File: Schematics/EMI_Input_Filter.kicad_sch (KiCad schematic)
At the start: 3 parts

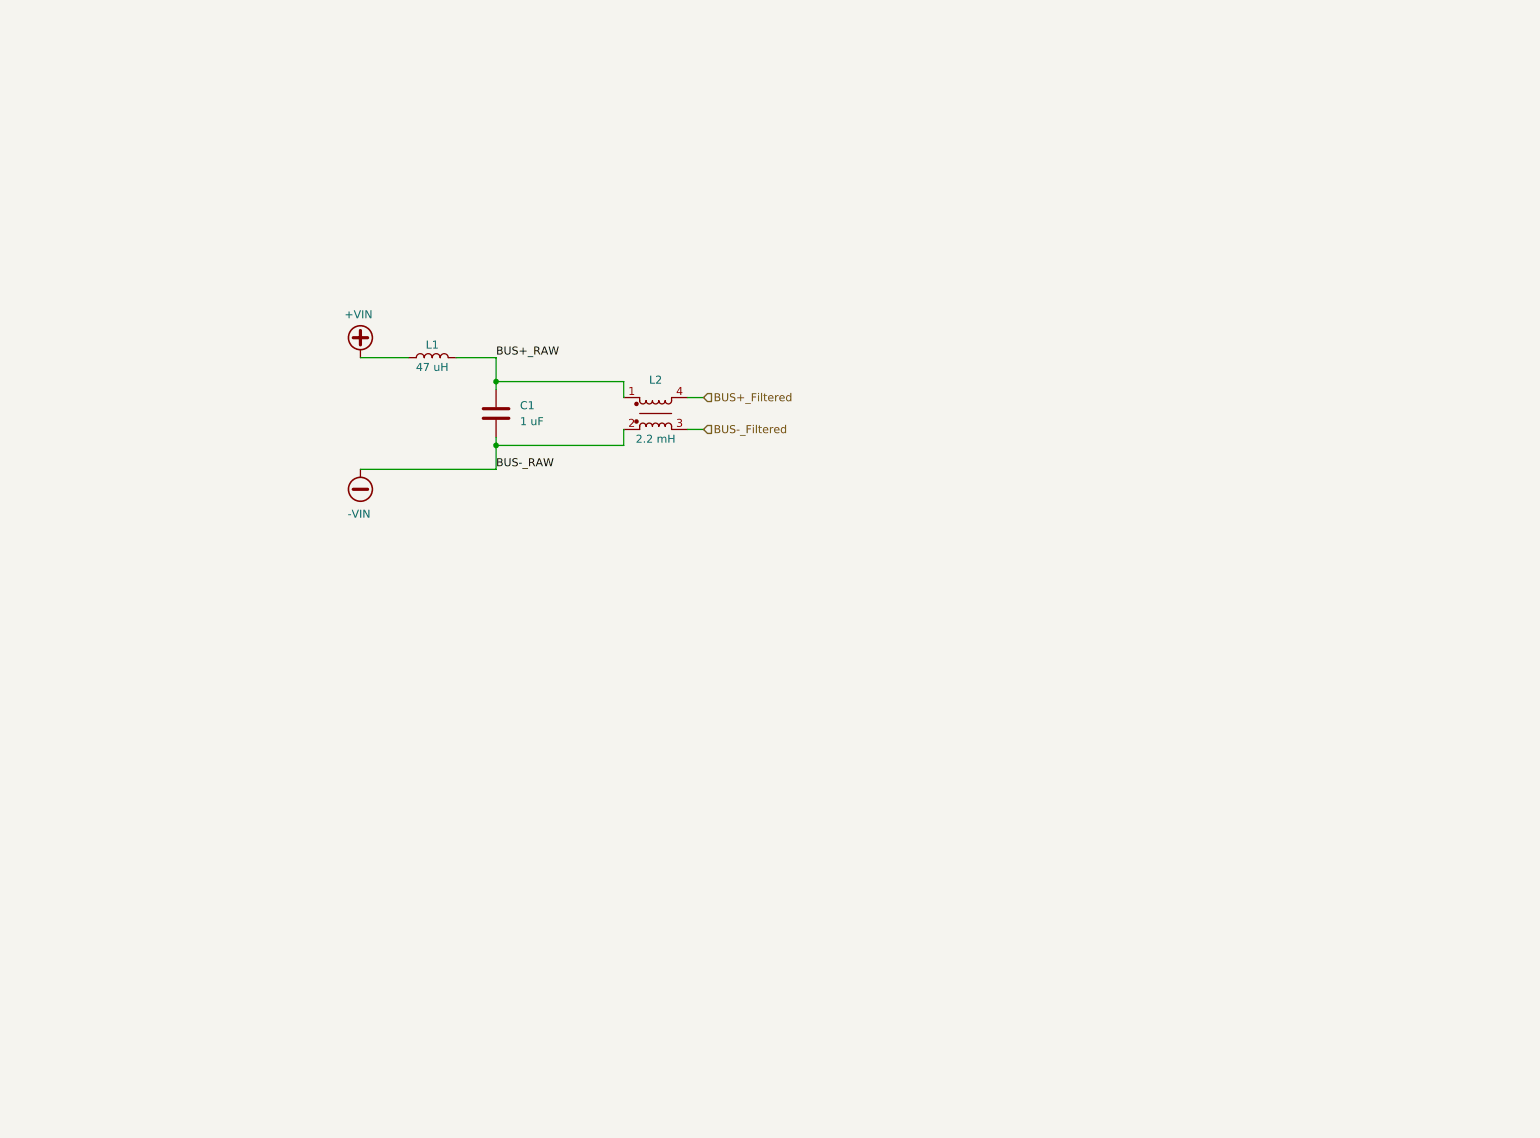
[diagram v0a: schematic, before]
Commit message: [SiC Inverter WIP]
- Deleted backup files
- changed symbol and footprint lib locations
- added text discription explaining the DC link sub sheet and emi  input
  filter subsheet
- Added Vin+,- Black and Red connector
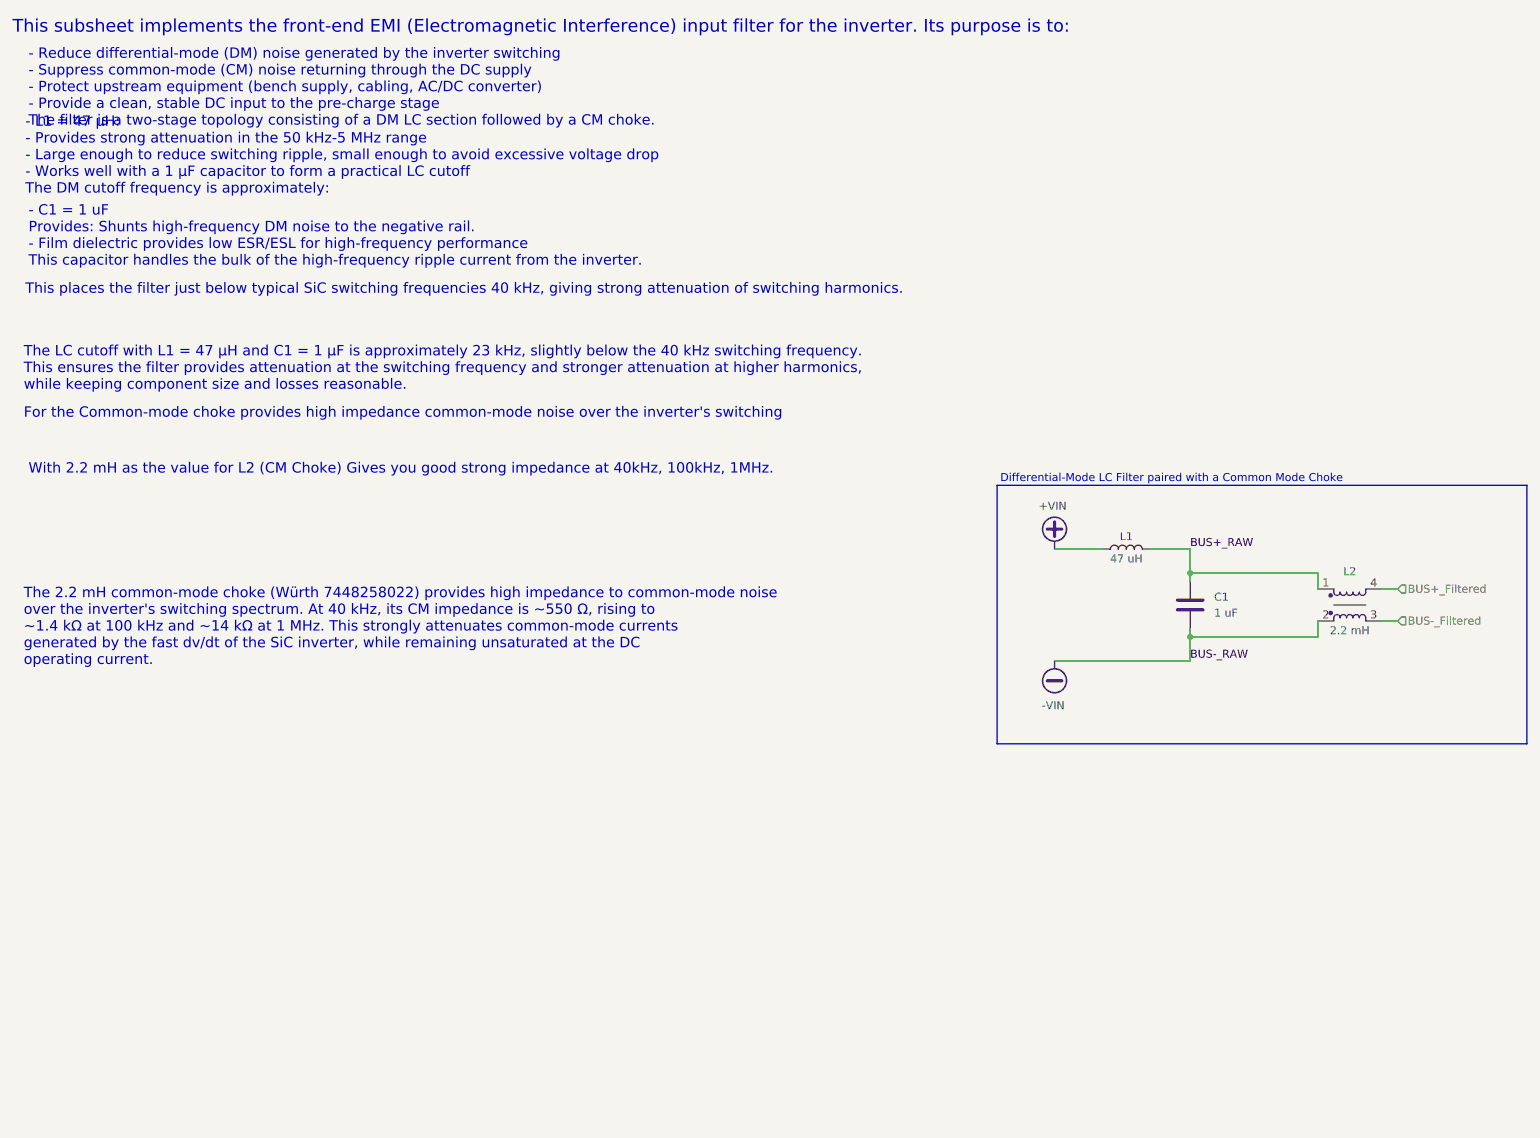
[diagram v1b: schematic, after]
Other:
- note added: "- C1 = 1 uF Provides: Shunts high‑frequency DM noise to the negative rail. - Film dielectric provides low ESR/ESL for high‑frequency performance This capacitor handles the bulk of the high‑frequency ripple current from the inverter."
- note added: "- L1 = 47 µH: - Provides strong attenuation in the 50 kHz-5 MHz range - Large enough to reduce switching ripple, small enough to avoid excessive voltage drop - Works well with a 1 µF capacitor to form a practical LC cutoff The DM cutoff frequency is approximately: This places the filter just below typical SiC switching frequencies 40 kHz, giving strong attenuation of switching harmonics."
- note added: "- Reduce differential‑mode (DM) noise generated by the inverter switching - Suppress common‑mode (CM) noise returning through the DC supply - Protect upstream equipment (bench supply, cabling, AC/DC converter) - Provide a clean, stable DC input to the pre‑charge stage The filter is a two‑stage topology consisting of a DM LC section followed by a CM choke."
- note added: "Differential-Mode LC Filter paired with a Common Mode Choke"
- note added: "For the Common-mode choke provides high impedance common-mode noise over the inverter's switching"
- note added: "The 2.2 mH common‑mode choke (Würth 7448258022) provides high impedance to common‑mode noise over the inverter's switching spectrum. At 40 kHz, its CM impedance is ~550 Ω, rising to ~1.4 kΩ at 100 kHz and ~14 kΩ at 1 MHz. This strongly attenuates common‑mode currents generated by the fast dv/dt of the SiC inverter, while remaining unsaturated at the DC operating current."
- note added: "The LC cutoff with L1 = 47 µH and C1 = 1 µF is approximately 23 kHz, slightly below the 40 kHz switching frequency. This ensures the filter provides attenuation at the switching frequency and stronger attenuation at higher harmonics, while keeping component size and losses reasonable."
- note added: "This subsheet implements the front‑end EMI (Electromagnetic Interference) input filter for the inverter. Its purpose is to:"
- note added: "With 2.2 mH as the value for L2 (CM Choke) Gives you good strong impedance at 40kHz, 100kHz, 1MHz."
- moved on the sheet: C1, L1, L2

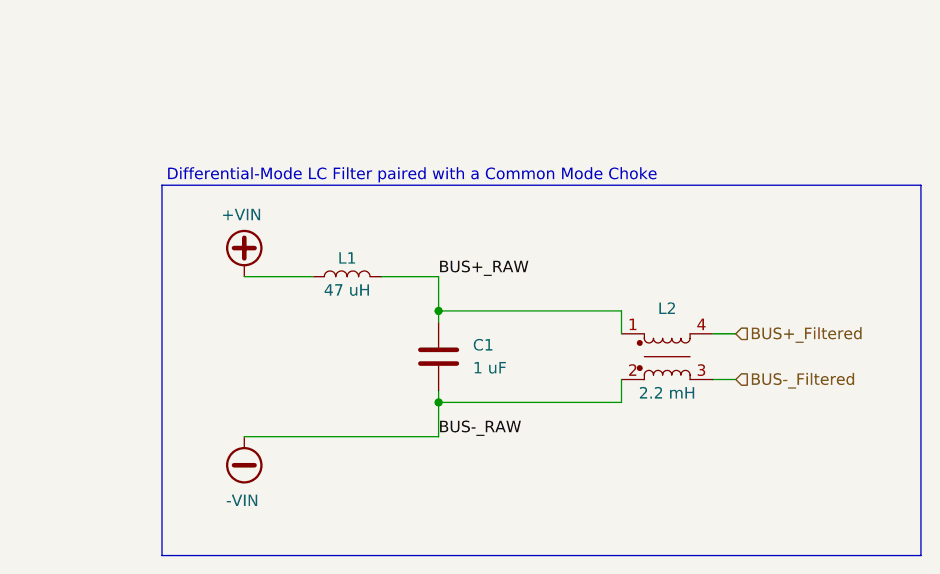
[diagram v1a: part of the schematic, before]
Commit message: Work in progress
- Added new parts to PCB to check 3d models
- Added input protection sheet
- Added TVS, N-Channel MOSFET, Zensor, and resiters to protection
  circuit
- Added datasheets for new parts
- Added circuit GND
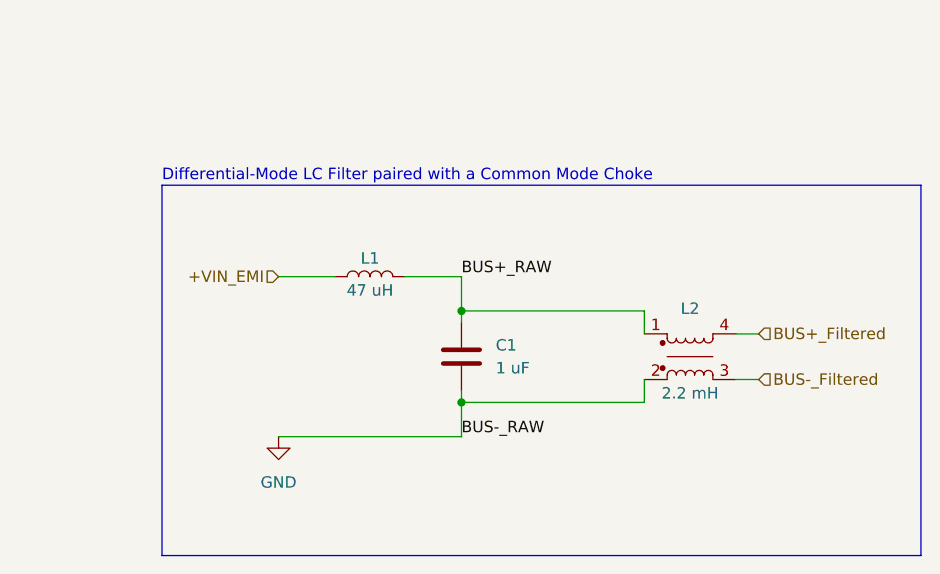
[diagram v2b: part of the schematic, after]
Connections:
- net +VIN renamed +VIN_EMI
- net -VIN renamed GND
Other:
- moved on the sheet: C1, L1, L2

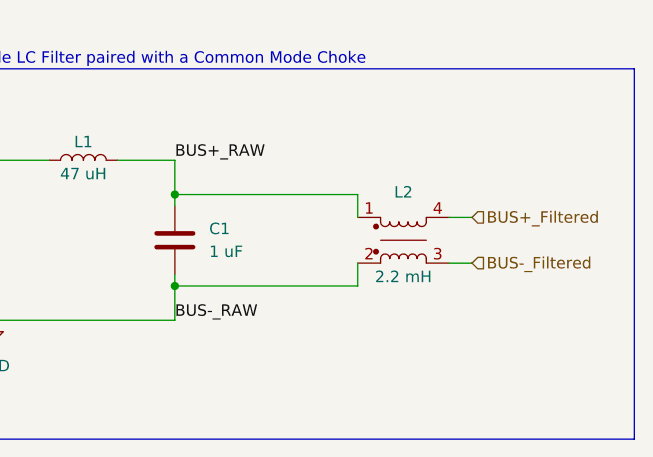
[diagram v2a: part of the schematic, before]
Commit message: [WIP - SIC Inverter]
- Added 3d models for 3 parts
- Added 3 new footprints for the 3 added parts
- Changed footprint 23AH8785 and 86 Black and Red
- Finished WIP with EMI, Input Protection, and Precharge
- Added datasheet
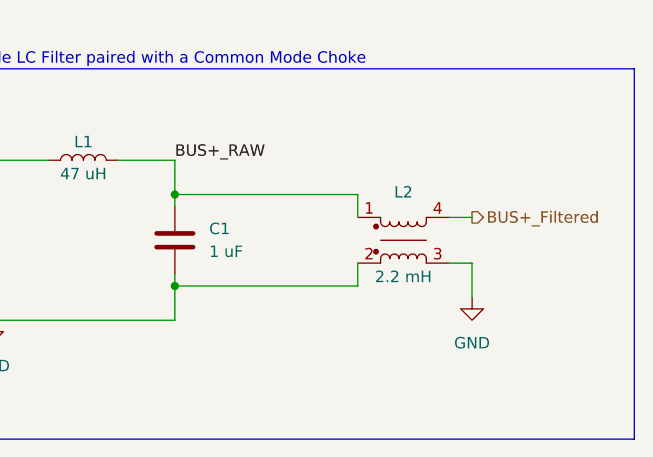
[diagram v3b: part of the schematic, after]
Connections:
- net BUS-_Filtered is gone; now on net GND: L2.3
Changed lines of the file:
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@@
+		)
+	)
+	(wire
+		(pts
+			(xy 236.22 114.3) (xy 236.22 110.49)
+		)
+		(stroke
+			(width 0)
+			(type default)
 		)
 	)
@@
 		)
 	)
-	(label "BUS-_RAW"
-		(at 203.2 116.84 0)
-		(effects
-			(font
-				(size 1.27 1.27)
-			)
-			(justify left bottom)
-		)
-	)
 	(label "BUS+_RAW"
 		(at 203.2 99.06 0)
@@
 		)
 	)
-	(hierarchical_label "BUS-_Filtered"
-		(shape input)
-		(at 236.22 110.49 0)
-		(effects
-			(font
-				(size 1.27 1.27)
-			)
-			(justify left)
-		)
-	)
 	(hierarchical_label "BUS+_Filtered"
-		(shape input)
+		(shape output)
 		(at 236.22 105.41 0)
 		(effects
@@
 					(unit 1)
 				)
+			)
+		)
+	)
+	(symbol
+		(lib_id "power:GND")
+		(at 236.22 114.3 0)
+		(unit 1)
+		(exclude_from_sim no)
+		(in_bom yes)
+		(on_board yes)
+		(dnp no)
+		(fields_autoplaced yes)
+		(property "Reference" "#PWR07"
+			(at 236.22 120.65 0)
+			(effects
+				(font
+					(size 1.27 1.27)
+				)
+				(hide yes)
+			)
+		)
+		(property "Value" "GND"
+			(at 236.22 119.38 0)
+			(effects
+				(font
+					(size 1.27 1.27)
+				)
+			)
+		)
+		(property "Footprint" ""
+			(at 236.22 114.3 0)
+			(effects
+				(font
+					(size 1.27 1.27)
+				)
+				(hide yes)
+			)
+		)
+		(property "Datasheet" ""
+			(at 236.22 114.3 0)
+			(effects
+				(font
+					(size 1.27 1.27)
+				)
+				(hide yes)
+			)
+		)
+		(property "Description" "Power symbol creates a global label with name \"GND\" , ground"
+			(at 236.22 114.3 0)
+			(effects
+				(font
+					(size 1.27 1.27)
+				)
+				(hide yes)
+			)
+		)
+		(pin "1"
+		)
+		(instances
+			(project "SiC_Single_Phase_Inverter"
+				(path "/a1ed0539-9735-4ad1-a8fd-87e26e7fce16/7998be36-55a1-424f-a315-c3fdbc8a6aca"
+					(reference "#PWR07")
+					(unit 1)
+				)
